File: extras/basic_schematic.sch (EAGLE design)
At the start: 18 parts, among them IC1 MCP23008/SO, M1 ARDUINO-PRO-MINI-3.3V

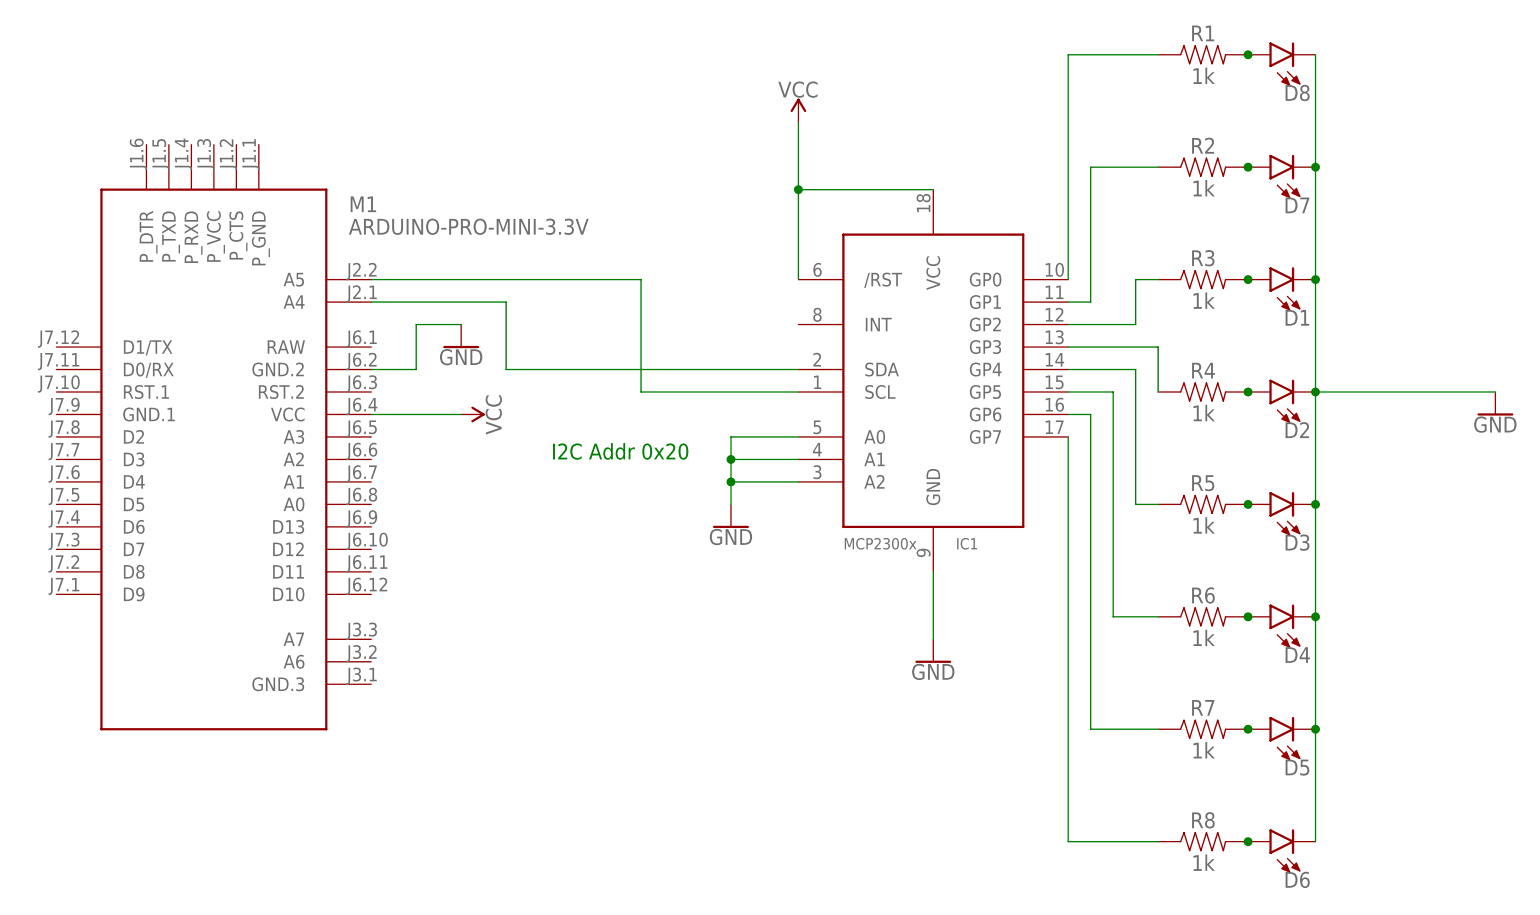
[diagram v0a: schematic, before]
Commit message: MCP23008 Arduino Library
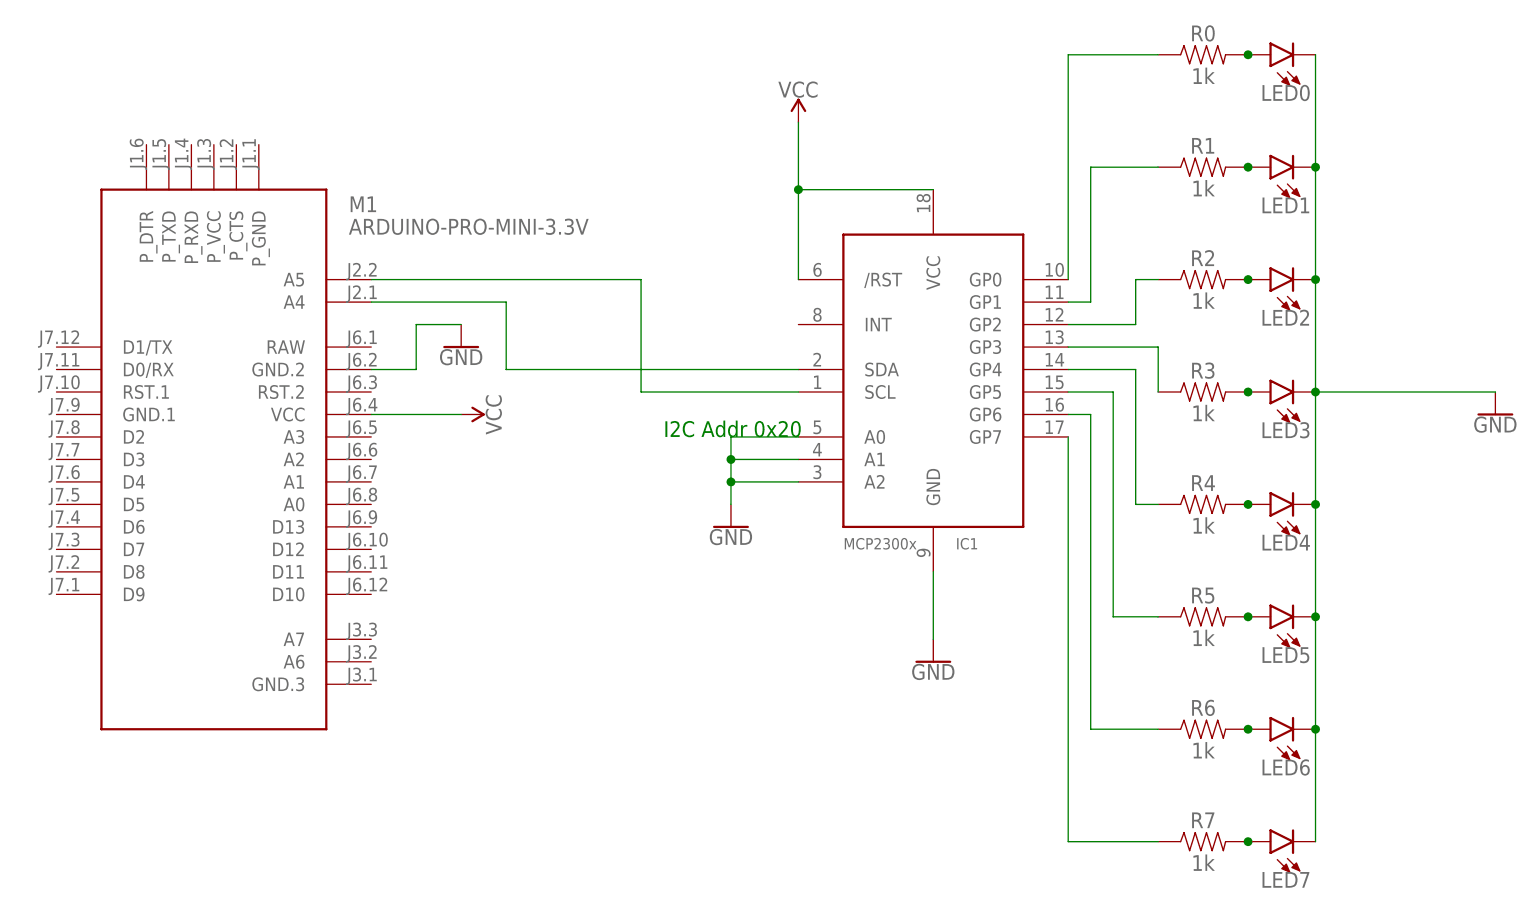
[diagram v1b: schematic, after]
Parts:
- removed R8: 1k, SparkFun-Resistors:1KOHM-0603-1/10W-1%
- added R0: 1k, SparkFun-Resistors:1KOHM-0603-1/10W-1%
- renumbered D1 to LED2, D2 to LED3, D3 to LED4, D4 to LED5, D5 to LED6, D6 to LED7, D7 to LED1, D8 to LED0
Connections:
- net N$10: now also R1.2; no longer R2.2
- net N$11: now also R0.1; no longer R1.1
- net N$12: now also R1.1; no longer R2.1
- net N$13: now also R2.1; no longer R3.1
- net N$14: now also R3.1; no longer R4.1
- net N$15: now also R4.1; no longer R5.1
- net N$16: now also R5.1; no longer R6.1
- net N$17: now also R6.1; no longer R7.1
- net N$18: now also R7.1; no longer R8.1
- net N$3: now also R0.2; no longer R1.2
- net N$4: now also R2.2; no longer R3.2
- net N$5: now also R3.2; no longer R4.2
- net N$6: now also R4.2; no longer R5.2
- net N$7: now also R5.2; no longer R6.2
- net N$8: now also R6.2; no longer R7.2
- net N$9: now also R7.2; no longer R8.2
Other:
- moved on the sheet: R1, R2, R3, R4, R5, R6, R7
